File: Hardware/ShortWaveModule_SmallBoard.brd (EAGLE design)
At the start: 36.8 x 31.8 mm, 54 parts, among them J1 CONN_42.54_SCREW, J2 CONN_42.54, J3 CONN_42.54, J4 CONN_42.54, Q1 2N7002, Q2 2N7002, Q3 DMG3404

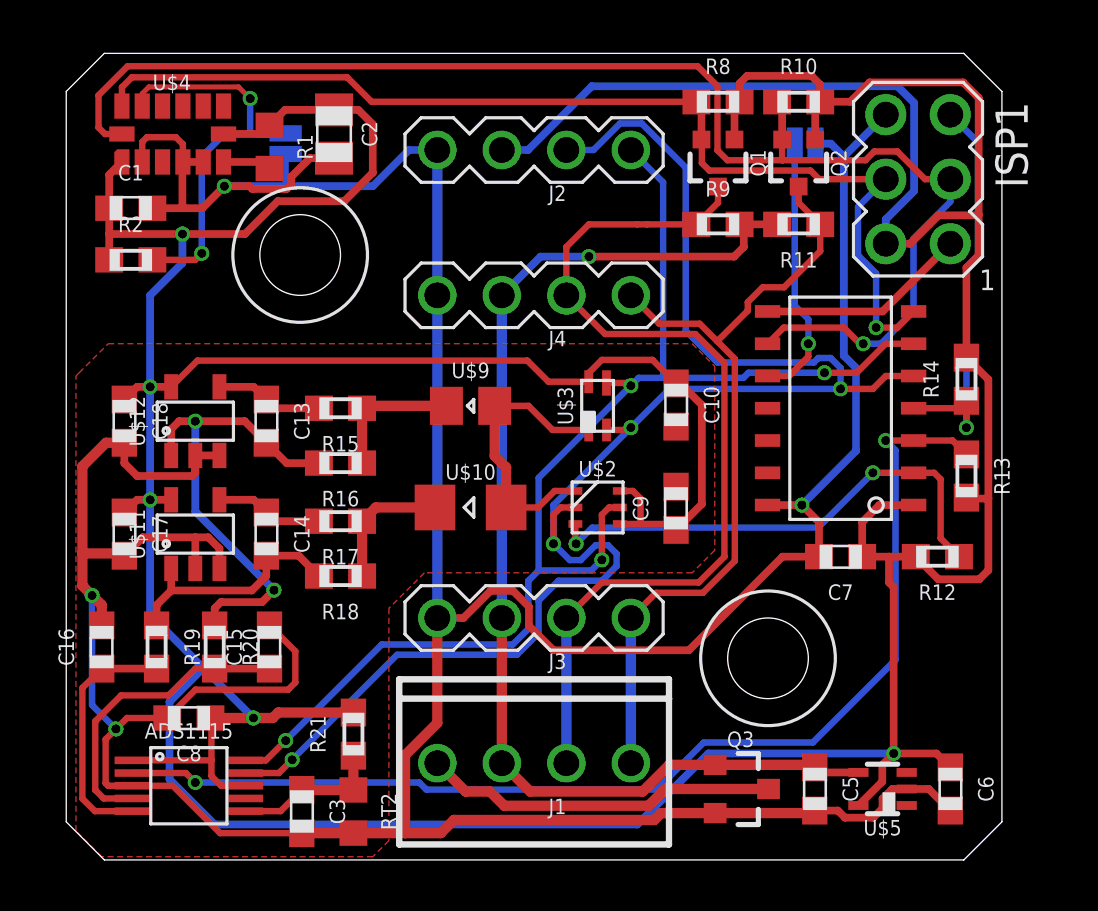
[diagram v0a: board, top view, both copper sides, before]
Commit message: Added pullups to shortwave module
Added pullups to onboard I2C on shortwave module, still need to fix silk screen and update parts before ready to ship
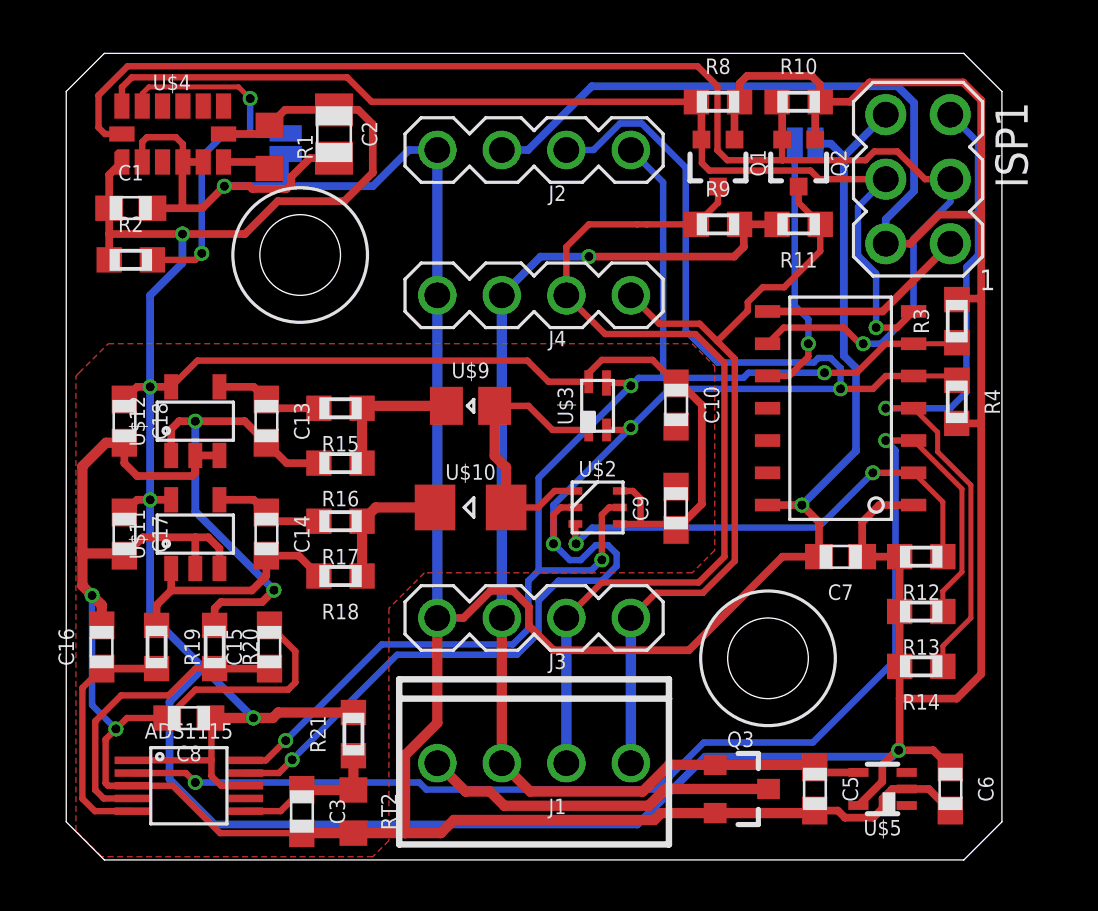
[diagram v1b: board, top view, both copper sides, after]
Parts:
- added R3, R4: 10k, bschulz_passives:R0603
- U$11, U$12: value LTC2054HV -> LTC2050
- moved R14 11.4 mm to (33.7, 7.62), turned to 180 degrees
- moved R13 5.62 mm to (33.7, 9.78), turned to 180 degrees
- moved R12 0.63 mm to (33.7, 11.9)
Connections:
- net 3V3: now also R3.2, R4.2
- net SCL: now also R3.1
- net SDA: now also R4.1
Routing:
- net !RESET: track 16.2 -> 27.7 mm
- net !ADC_INT: track 44.6 -> 50.1 mm
- net 3V3: track 214.4 -> 219.3 mm
- net SDA: track 63.3 -> 65.2 mm
- net SCL: track 52.1 -> 53.8 mm
- net !LUX_INT: track 19.9 -> 19.2 mm

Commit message: Updated parts and BOM
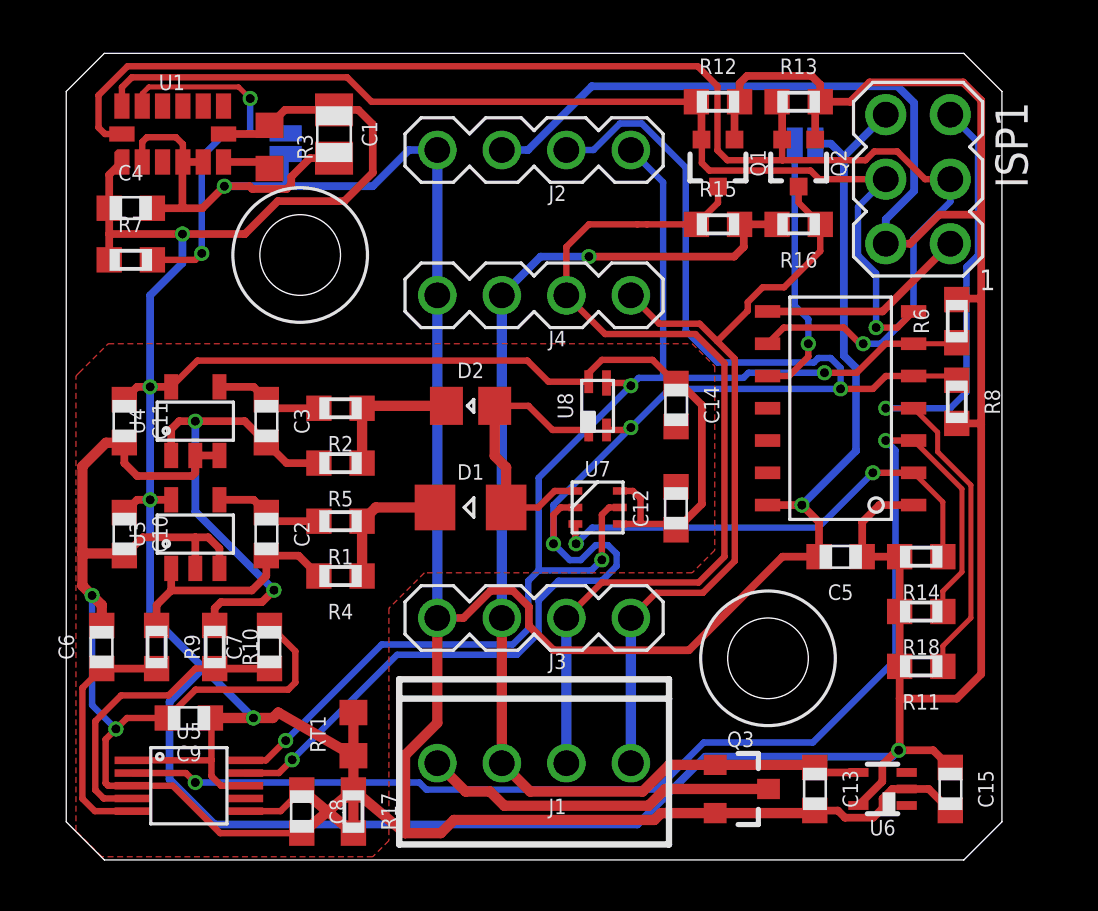
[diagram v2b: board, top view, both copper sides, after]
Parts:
- removed C16: 1uF, bschulz_passives:C0603
- removed C17: 0.1uF, bschulz_passives:C0603
- removed H3: (no value), bschulz:4_40
- removed R19, R20: 1k, bschulz_passives:R0603
- removed R21: 10k, bschulz_passives:R0603
- removed RT2: (no value), bschulz:R0603
- added C12, C4: 0.1uF, bschulz_passives:C0603
- added H2: (no value), bschulz:4_40
- added R5, R6, R7: 10k, bschulz_passives:R0603
- added RT1: 10k, bschulz:R0603
- C1: value 0.1uF -> 10uF; device bschulz_passives:C0603 -> bschulz_passives:C0805
- C13: value 0.15uF -> 1uF
- C14: value 0.15uF -> 0.1uF
- C2: value 10uF -> 0.15uF; device bschulz_passives:C0805 -> bschulz_passives:C0603
- C3: value 0.1uF -> 0.15uF
- C5: value 1uF -> 0.1uF
- C7: value 0.1uF -> 1uF
- R1: value 27R -> 1k; device bschulz:R0603 -> bschulz_passives:R0603
- R10, R2, R9: value 10k -> 1k
- R15, R17: value 1k -> 10k
- R16: value 47k -> 10k
- R18: value 1M -> 10k
- R3: value 10k -> 27R; device bschulz_passives:R0603 -> bschulz:R0603
- R4: value 10k -> 100k
- moved C6 33.9 mm to (1.40, 8.38), turned to 90 degrees
- moved R10 31.4 mm to (5.84, 8.38), turned to 270 degrees
- moved R3 27.9 mm to (8.00, 28.1), turned to 270 degrees
- moved R9 27.7 mm to (3.56, 8.38), turned to 270 degrees
- moved C15 27.4 mm to (34.8, 2.79), turned to 270 degrees
- moved C13 26.0 mm to (29.5, 2.79)
- moved R4 25.2 mm to (10.8, 11.2), turned to 180 degrees
- moved H1 24.3 mm to (27.6, 7.94)
- moved R18 22.9 mm to (33.7, 9.78)
- moved C7 22.8 mm to (8.00, 8.38), turned to 90 degrees
- moved C10 22.3 mm to (2.29, 12.8)
- moved C9 20.9 mm to (4.83, 5.59), turned to 180 degrees
- moved R13 20.6 mm to (28.8, 29.8), turned to 0 degrees
- moved R16 20.3 mm to (28.8, 25.0)
- moved R12 19.6 mm to (25.7, 29.8), turned to 0 degrees
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- renumbered ADS1115 to U5, C18 to C11, U$1 to U2, U$10 to D1, U$11 to U3, U$12 to U4, U$2 to U7, U$3 to U8, U$4 to U1, U$5 to U6, U$9 to D2
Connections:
- net !ADC_INT: now also R18.1; no longer R13.1
- net !LUX_INT: now also R14.1; no longer R12.1
- net !RESET: now also R11.1; no longer R14.1
- net 3V3: now also C12.1, C14.1, C15.1, C4.1, C5.1, R11.2, R18.2, R3.1, R6.2, R7.1, RT1.1; no longer C17.1, C2.1, C6.1, C7.1, C8.1, R1.1, R10.2, R2.1, R21.2, R3.2, R4.2
- net AOUT_MWAVE: now also C6.1, R9.2; no longer C16.1, R19.2
- net AOUT_SWAVE: now also C7.1, R10.2; no longer C15.1, R20.2
- net AOUT_THERM: now also C8.1, R17.2, RT1.2; no longer C3.1, R21.1, RT2.1
- net GND: now also C12.2, C13.2, C14.2, C4.2, R17.1; no longer C16.2, C17.2, C2.2, C3.2, RT2.2
- net N$1: now also R7.2; no longer R2.2
- net N$10: now also R1.1, R4.1; no longer R17.1, R18.1
- net N$11: now also C2.1, R1.2; no longer C14.1, R17.2
- net N$12: now also C2.2, R4.2, R9.1; no longer C14.2, R18.2, R19.1
- net N$13: now also C3.2, R10.1, R5.2; no longer C13.2, R16.2, R20.1
- net N$8: now also C3.1, R2.2; no longer C13.1, R15.2
- net N$9: now also R2.1, R5.1; no longer R15.1, R16.1
- net SCL: now also R6.1; no longer R3.1
- net SCL_EXT: now also R13.1; no longer R10.1
- net SCL_EXT_HV: now also R16.1; no longer R11.1
- net SDA: now also R8.1; no longer R4.1
- net SDA_EXT: now also R12.1; no longer R8.1
- net SDA_EXT_HV: now also R15.1; no longer R9.1
- net VIN+: now also C13.1, R15.2, R16.2; no longer C5.1, R11.2, R9.2
- net VS: now also R3.2; no longer R1.2
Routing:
- net AOUT_THERM: track 5.97 -> 9.99 mm
- net GND: track 180.2 -> 181.4 mm
